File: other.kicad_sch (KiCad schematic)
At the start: 14 parts, among them J1 SSD1306, SW2 SW_Push, SW3 SW_Push, SW4 SW_Push, U6 W25Q80DVSSIG, U7 OPT3001DNPRQ1

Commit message: Organized components in pcb layout editor
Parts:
- removed R1, R2: 4.7kΩ, Resistor_SMD:R_0402_1005Metric, symbol Device:R
- J1: footprint 1_I-SYST_inc:OLED_1.3in_I2C -> 1_I_Syst.inc:OLED_1.3in_I2C; Price (none) -> 10.98
- SW2, SW3, SW4: footprint Button_Switch_SMD:SW_Push_1P1T_NO_CK_KSC7xxJ -> Button_Switch_SMD:SW_Push_1P1T-MP_NO_Horizontal_Alps_SKRTLAE010
- U6: footprint 1_I-SYST_inc:WIN_SS-8_WIN-L -> 1_I_Syst.inc:WIN_SS-8_WIN-L
- U7: footprint 1_I-SYST_inc:SON65P200X200X65-7N -> 1_I_Syst.inc:SON65P200X200X65-7N
- renumbered R9 to R6
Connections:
- net P0.09 renamed P2.00
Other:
- moved on the sheet: C12, C4, C5, C6, R6, SW2, SW3, SW4, U6

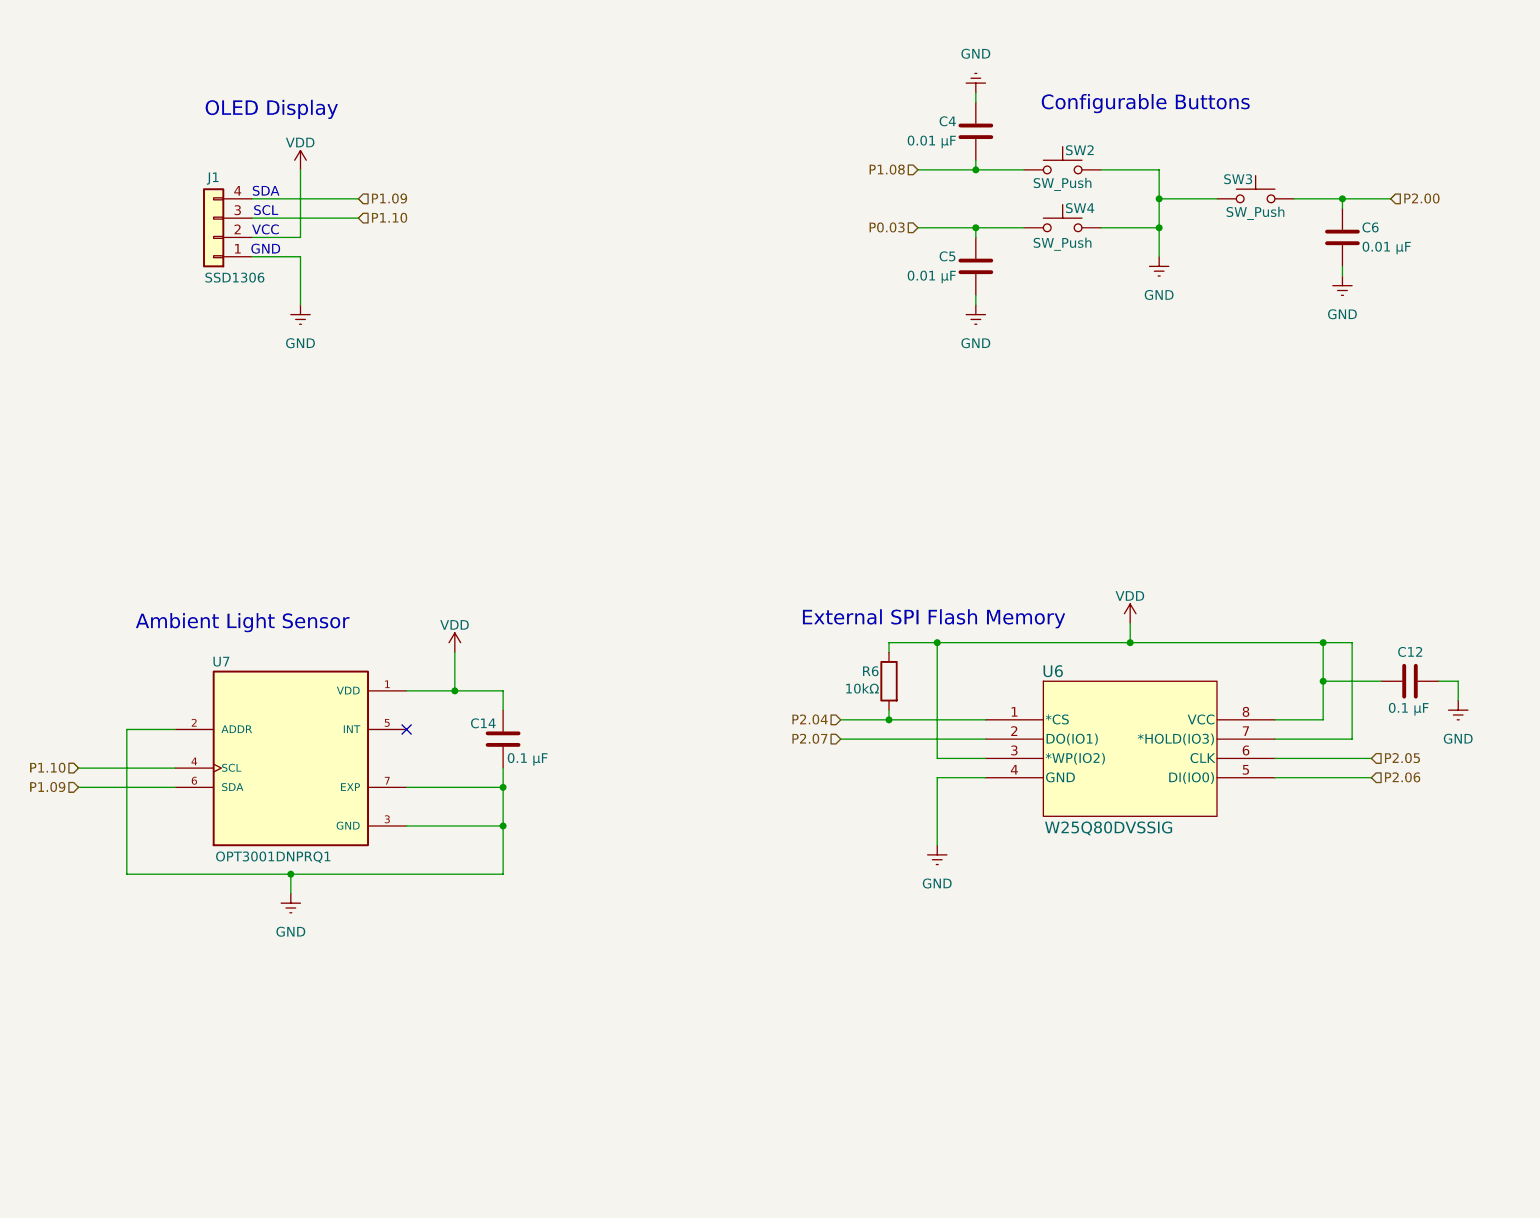
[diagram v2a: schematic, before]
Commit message: Full Redesign of the Watch PCB (DRC still not fully passed)
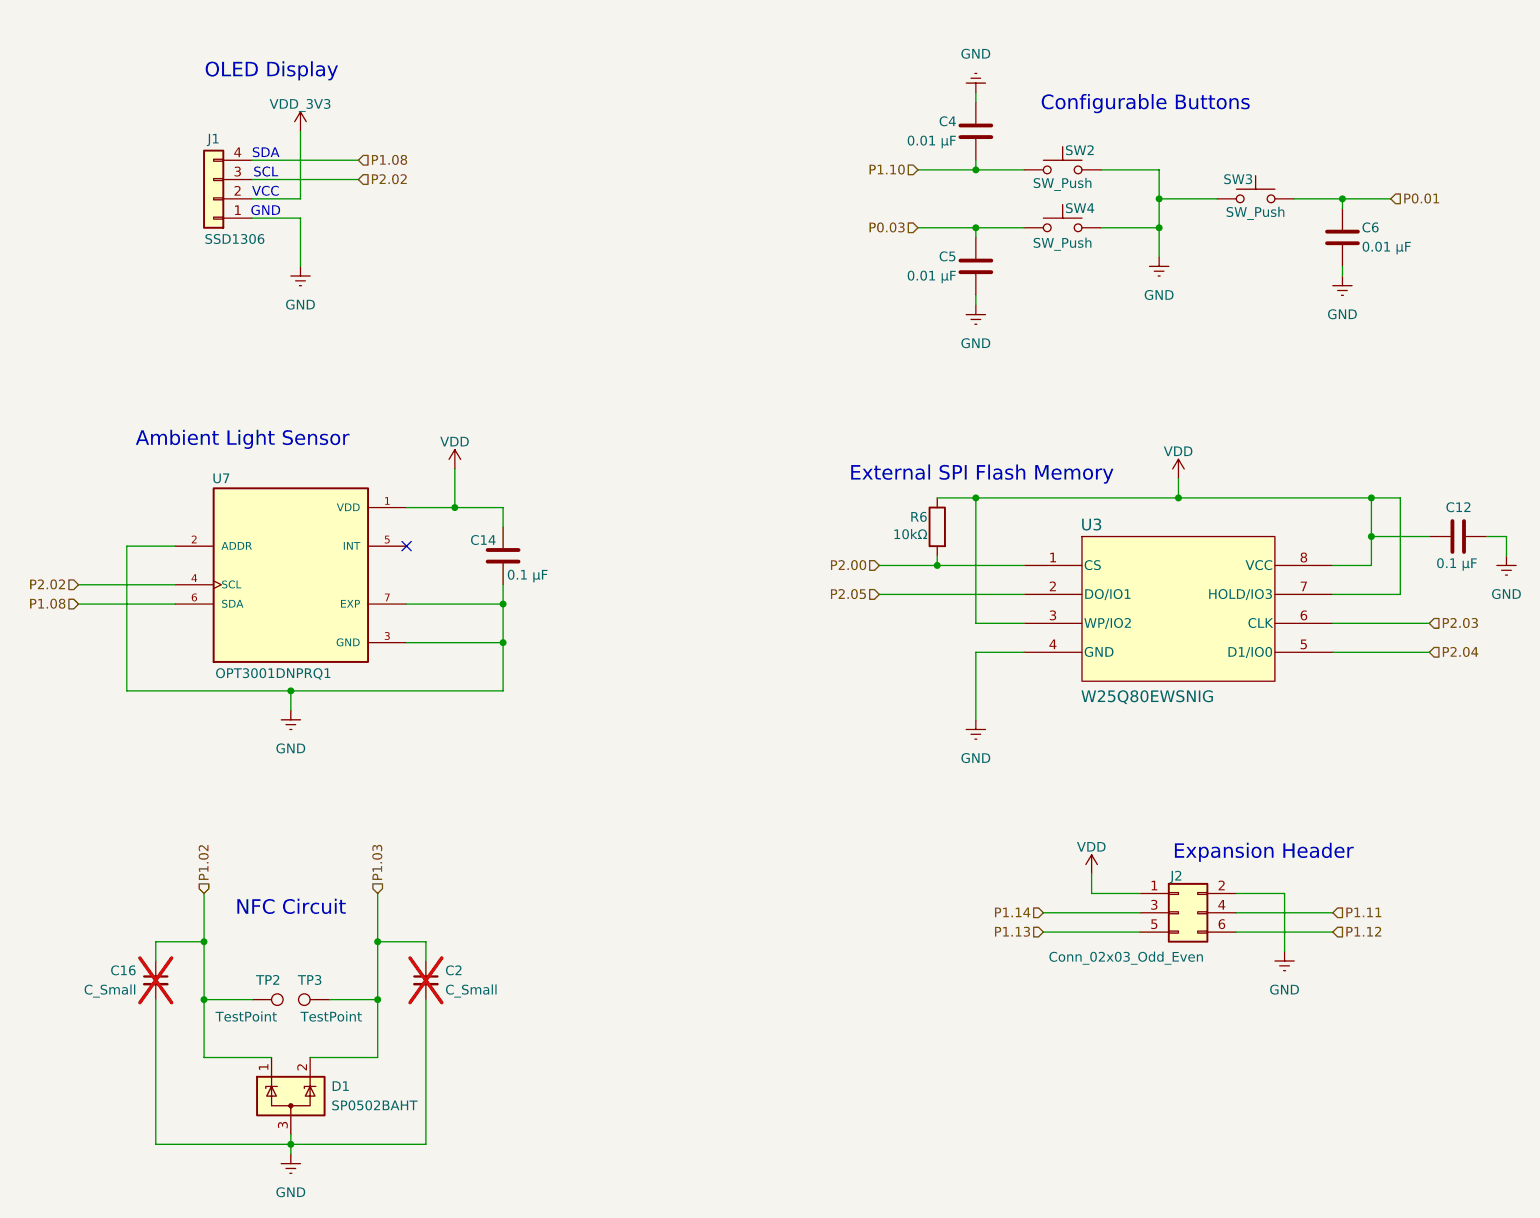
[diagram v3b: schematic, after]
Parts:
- removed U6: W25Q80DVSSIG, 1_I_Syst.inc:WIN_SS-8_WIN-L, symbol I_Syst_inc:W25Q80DVSSIG
- added C16, C2: C_Small, Capacitor_SMD:C_0603_1608Metric_Pad1.08x0.95mm_HandSolder, symbol Device:C_Small
- added D1: SP0502BAHT, Package_TO_SOT_SMD:SOT-23, symbol Power_Protection:SP0502BAHT
- added J2: Conn_02x03_Odd_Even, Connector_PinHeader_1.27mm:PinHeader_2x03_P1.27mm_Vertical_SMD, symbol Connector_Generic:Conn_02x03_Odd_Even
- added TP2, TP3: TestPoint, TestPoint:TestPoint_Pad_D1.0mm, symbol Connector:TestPoint
- added U3: W25Q80EWSNIG, 1_I_Syst.inc:W25Q80EWSNIG_WIN-M, symbol 1_I_Syst.inc:W25Q80EWSNIG
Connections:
- net P1.09 is gone; now on net P1.08: J1.4 (Pin_4), U7.6 (SDA)
- net GND: now also C16.2, C2.2, D1.3 (A), J2.2 (Pin_2), U3.4 (GND)
- net P1.08: no longer C4.2, SW2.1
- net P1.10: now also C4.2, SW2.1; no longer J1.3 (Pin_3), U7.4 (SCL)
- net P2.00: now also R6.2, U3.1 (CS); no longer C6.1, SW3.1
- net P2.04: now also U3.5 (D1/IO0); no longer R6.2
- net P2.05: now also U3.2 (DO/IO1)
- net VDD: now also J2.1 (Pin_1), U3.3 (WP/IO2), U3.7 (HOLD/IO3), U3.8 (VCC); no longer J1.2 (Pin_2)
- new net P0.01: C6.1, SW3.1
- new net P1.02: C16.1, D1.1 (K), TP2.1
- new net P1.03: C2.1, D1.2 (K), TP3.1
- new net P1.11: J2.4 (Pin_4)
- new net P1.12: J2.6 (Pin_6)
- new net P1.13: J2.5 (Pin_5)
- new net P1.14: J2.3 (Pin_3)
- new net P2.02: J1.3 (Pin_3), U7.4 (SCL)
- new net P2.03: U3.6 (CLK)
- new net VDD_3V3: J1.2 (Pin_2)
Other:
- note added: "Expansion Header"
- note added: "NFC Circuit"
- moved on the sheet: C12, C14, J1, R6, U7
